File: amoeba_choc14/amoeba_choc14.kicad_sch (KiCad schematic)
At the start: 7 parts, among them J1 Conn_01x01_Pin, J2 Conn_01x01_Pin, J3 Conn_01x01_Pin, J4 Conn_01x01_Pin, J5 Conn_01x01_Pin, SW1 SW_SPST

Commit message: feat: use SOD-323 diode, as 123 out of stock
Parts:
- D1: footprint Diode_SMD:D_SOD-123 -> Diode_SMD:D_SOD-323_HandSoldering; LCSC C81598 -> C2128
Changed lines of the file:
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@@
 			)
 		)
-		(property "Footprint" "Diode_SMD:D_SOD-123"
+		(property "Footprint" "Diode_SMD:D_SOD-323_HandSoldering"
 			(at 139.7 102.87 0)
 			(effects
@@
 			)
 		)
-		(property "LCSC" "C81598"
+		(property "LCSC" "C2128"
 			(at 139.7 102.87 0)
 			(effects

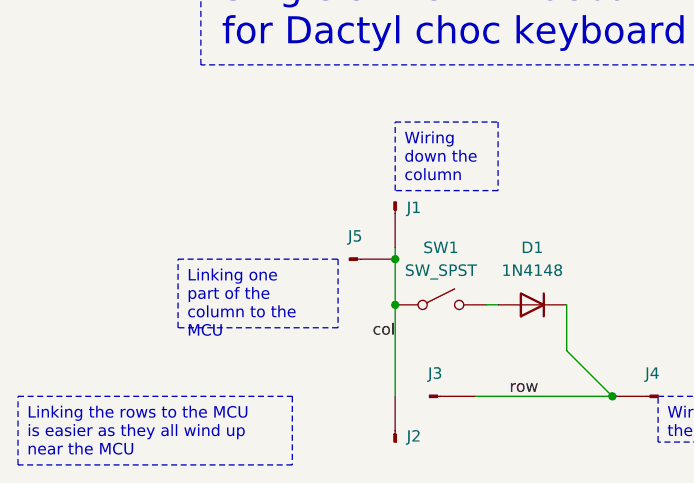
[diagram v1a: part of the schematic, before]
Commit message: feat: oval wire pads offset for easier curve
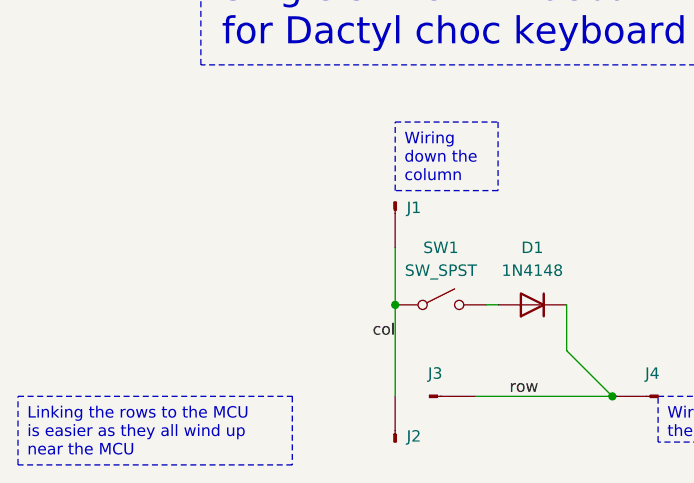
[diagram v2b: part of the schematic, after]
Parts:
- removed J5: Conn_01x01_Pin, Amoeba_Choc_Nar:Pin_D0.8mm_L7.0mm, symbol Connector:Conn_01x01_Pin
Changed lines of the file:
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@@
-	)
-	(junction
-		(at 124.46 97.79)
-		(diameter 0)
-		(color 0 0 0 0)
 	)
 	(junction
@@
 	(wire
 		(pts
-			(xy 124.46 96.52) (xy 124.46 97.79)
+			(xy 124.46 96.52) (xy 124.46 102.87)
 		)
 		(stroke
@@
 		(pts
 			(xy 124.46 102.87) (xy 124.46 113.03)
-		)
-		(stroke
-			(width 0)
-			(type default)
-		)
-	)
-	(wire
-		(pts
-			(xy 124.46 97.79) (xy 124.46 102.87)
 		)
 		(stroke
@@
 			(font
 				(size 4 4)
-			)
-			(justify left top)
-		)
-	)
-	(text_box "Linking one part of the column to the MCU"
-		(exclude_from_sim no)
-		(at 100.33 97.79 0)
-		(size 17.78 7.62)
-		(stroke
-			(width 0)
-			(type dot)
-		)
-		(fill
-			(type none)
-		)
-		(effects
-			(font
-				(size 1.27 1.27)
 			)
 			(justify left top)
@@
 					(unit 1)
 				)
-			)
-		)
-	)
-	(symbol
-		(lib_name "Conn_01x01_Pin_1")
-		(lib_id "Connector:Conn_01x01_Pin")
-		(at 119.38 97.79 0)
-		(unit 1)
-		(exclude_from_sim no)
-		(in_bom no)
-		(on_board yes)
-		(dnp no)
-		(fields_autoplaced yes)
-		(property "Reference" "J5"
-			(at 120.015 95.25 0)
-			(effects
-				(font
-					(size 1.27 1.27)
-				)
-			)
-		)
-		(property "Value" "Conn_01x01_Pin"
-			(at 121.285 96.52 90)
-			(effects
-				(font
-					(size 1.27 1.27)
-				)
-				(justify left)
-				(hide yes)
-			)
-		)
-		(property "Footprint" "Amoeba_Choc_Nar:Pin_D0.8mm_L7.0mm"
-			(at 119.38 97.79 0)
-			(effects
-				(font
-					(size 1.27 1.27)
-				)
-				(hide yes)
-			)
-		)
-		(property "Datasheet" "~"
-			(at 119.38 97.79 0)
-			(effects
-				(font
-					(size 1.27 1.27)
-				)
-				(hide yes)
-			)
-		)
-		(property "Description" ""
-			(at 119.38 97.79 0)
-			(effects
-				(font
-					(size 1.27 1.27)
-				)
-				(hide yes)
-			)
-		)
-		(property "Config" "do not fit"
-			(at 119.38 97.79 0)
-			(effects
-				(font
-					(size 1.27 1.27)
-				)
-				(hide yes)
-			)
-		)
-		(pin "1"
-		)
-		(instances
-			(project "amoeba_choc14"
-				(path "/c1f16e18-f6ca-463c-9cde-8f3fe4c41e25"
-					(reference "J5")
-					(unit 1)
-				)
